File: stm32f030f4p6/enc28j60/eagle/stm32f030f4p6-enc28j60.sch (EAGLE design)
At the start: 29 parts, among them IC2 LM1117IDTX-3.3, IC3 LP2950, X1 MINI-USB-UX60-MB-5ST

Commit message: updated stm32f030f4p6/enc28j60/eagle
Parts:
- added BOOT-SW: (no value), pinhead:PINHD-1X3
- added R1: 5K, resistor:R-EU_0204/5
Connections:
- net N$1 renamed VDDA
- net N$10 renamed PA3
- net N$11 renamed PA4@L
- net N$12 renamed PA5
- net N$13 renamed PA6
- net N$14 renamed PF1@LED
- net N$187 renamed 5V@EXT
- net N$188 renamed 3V3@EXT
- net N$19 renamed PF1@OCC
- net N$190 renamed PA7
- net N$20 renamed PF0@OCC
- net N$21 renamed RESET
- net N$23 renamed PA4@R
- net N$29 renamed PF0@LED
- net N$4 renamed PF0
- net N$5 renamed PF1
- net N$6 renamed PA4
- net N$7 renamed PA0
- net N$8 renamed PA1
- net N$9 renamed PA2
- removed net N$3: STM32F030F4PX_L.1, STM32F030F4PX_L.2
- new net BOOT: R1.1, STM32F030F4PX_L.1, STM32F030F4PX_L.2
- new net N$1: BOOT-SW.2, R1.2
- net GND@0: now also BOOT-SW.1
- net VDD: now also BOOT-SW.3
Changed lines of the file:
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@@
 <part name="LED3" library="eagle-ltspice" deviceset="LED_E" device="LD260"/>
 <part name="LED1_R1" library="resistor" deviceset="R-EU_" device="0204/7"/>
+<part name="BOOT-SW" library="pinhead" deviceset="PINHD-1X3" device=""/>
+<part name="R1" library="resistor" deviceset="R-EU_" device="0204/5" value="5K"/>
 </parts>
 <sheets>
@@
 <instance part="LED3" gate="G$1" x="124.46" y="93.98"/>
 <instance part="LED1_R1" gate="G$1" x="119.38" y="88.9"/>
+<instance part="BOOT-SW" gate="A" x="119.38" y="33.02" rot="R90"/>
+<instance part="R1" gate="G$1" x="116.84" y="35.56"/>
 </instances>
 <busses>
 </busses>
 <nets>
-<net name="N$1" class="0">
+<net name="VDDA" class="0">
 <segment>
 <pinref part="STM32F030F4PX_L" gate="A" pin="9"/>
@@
 </segment>
 </net>
-<net name="N$3" class="0">
+<net name="BOOT" class="0">
 <segment>
 <pinref part="STM32F030F4PX_L" gate="A" pin="1"/>
 <pinref part="STM32F030F4PX_L" gate="A" pin="2"/>
-<wire x1="101.6" y1="53.34" x2="106.68" y2="53.34" width="0.1524" layer="91"/>
-<wire x1="99.06" y1="53.34" x2="101.6" y2="53.34" width="0.1524" layer="91"/>
+<wire x1="99.06" y1="53.34" x2="106.68" y2="53.34" width="0.1524" layer="91"/>
 <junction x="99.06" y="53.34"/>
 <junction x="106.68" y="53.34"/>
-</segment>
-</net>
-<net name="N$4" class="0">
+<wire x1="106.68" y1="53.34" x2="111.76" y2="53.34" width="0.1524" layer="91"/>
+<wire x1="111.76" y1="53.34" x2="111.76" y2="35.56" width="0.1524" layer="91"/>
+<pinref part="R1" gate="G$1" pin="1"/>
+</segment>
+</net>
+<net name="PF0" class="0">
 <segment>
 <pinref part="STM32F030F4PX_L" gate="A" pin="4"/>
@@
 </segment>
 </net>
-<net name="N$5" class="0">
+<net name="PF1" class="0">
 <segment>
 <pinref part="STM32F030F4PX_L" gate="A" pin="5"/>
@@
 </segment>
 </net>
-<net name="N$7" class="0">
+<net name="PA0" class="0">
 <segment>
 <pinref part="STM32F030F4PX_L" gate="A" pin="12"/>
@@
 </segment>
 </net>
-<net name="N$8" class="0">
+<net name="PA1" class="0">
 <segment>
 <pinref part="STM32F030F4PX_L" gate="A" pin="13"/>
@@
 </segment>
 </net>
-<net name="N$9" class="0">
+<net name="PA2" class="0">
 <segment>
 <pinref part="STM32F030F4PX_L" gate="A" pin="16"/>
@@
 </segment>
 </net>
-<net name="N$10" class="0">
+<net name="PA3" class="0">
 <segment>
 <pinref part="STM32F030F4PX_L" gate="A" pin="17"/>
@@
 </segment>
 </net>
-<net name="N$11" class="0">
+<net name="PA4@L" class="0">
 <segment>
 <wire x1="99.06" y1="-7.62" x2="5.08" y2="-7.62" width="0.1524" layer="91"/>
@@
 </segment>
 </net>
-<net name="N$12" class="0">
+<net name="PA5" class="0">
 <segment>
 <pinref part="STM32F030F4PX_R" gate="A" pin="19"/>
@@
 </segment>
 </net>
-<net name="N$13" class="0">
+<net name="PA6" class="0">
 <segment>
 <pinref part="STM32F030F4PX_R" gate="A" pin="18"/>
@@
 </segment>
 </net>
-<net name="N$21" class="0">
+<net name="RESET" class="0">
 <segment>
 <pinref part="RST_S" gate="S" pin="2"/>
@@
 <wire x1="101.6" y1="66.04" x2="86.36" y2="66.04" width="0.1524" layer="91"/>
 <junction x="86.36" y="66.04"/>
-<wire x1="86.36" y1="25.4" x2="132.08" y2="25.4" width="0.1524" layer="91"/>
+<wire x1="86.36" y1="25.4" x2="116.84" y2="25.4" width="0.1524" layer="91"/>
+<wire x1="116.84" y1="25.4" x2="132.08" y2="25.4" width="0.1524" layer="91"/>
 <wire x1="132.08" y1="25.4" x2="132.08" y2="40.64" width="0.1524" layer="91"/>
 <junction x="86.36" y="25.4"/>
@@
 <pinref part="LED1_R1" gate="G$1" pin="1"/>
 <wire x1="114.3" y1="88.9" x2="109.22" y2="88.9" width="0.1524" layer="91"/>
+<pinref part="BOOT-SW" gate="A" pin="1"/>
+<wire x1="116.84" y1="30.48" x2="116.84" y2="25.4" width="0.1524" layer="91"/>
+<junction x="116.84" y="25.4"/>
 </segment>
 </net>
@@
 <pinref part="VDD{,A}" gate="G$1" pin="1"/>
 <pinref part="STM32F030F4PX_R" gate="A" pin="9"/>
-<wire x1="124.46" y1="43.18" x2="137.16" y2="43.18" width="0.1524" layer="91"/>
+<wire x1="124.46" y1="43.18" x2="129.54" y2="43.18" width="0.1524" layer="91"/>
 <pinref part="STM32F030F4PX_R" gate="A" pin="10"/>
+<wire x1="129.54" y1="43.18" x2="137.16" y2="43.18" width="0.1524" layer="91"/>
 <wire x1="137.16" y1="43.18" x2="144.78" y2="43.18" width="0.1524" layer="91"/>
 <junction x="137.16" y="43.18"/>
@@
 <pinref part="LED3" gate="G$1" pin="A"/>
 <junction x="124.46" y="96.52"/>
-</segment>
-</net>
-<net name="N$6" class="0">
+<pinref part="BOOT-SW" gate="A" pin="3"/>
+<wire x1="121.92" y1="30.48" x2="129.54" y2="30.48" width="0.1524" layer="91"/>
+<wire x1="129.54" y1="30.48" x2="129.54" y2="43.18" width="0.1524" layer="91"/>
+<junction x="129.54" y="43.18"/>
+</segment>
+</net>
+<net name="PA4" class="0">
 <segment>
 <pinref part="STM32F030F4PX_L" gate="A" pin="19"/>
@@
 </segment>
 </net>
-<net name="N$23" class="0">
+<net name="PA4@R" class="0">
 <segment>
 <pinref part="PA4_JP" gate="A" pin="3"/>
@@
 </segment>
 </net>
-<net name="N$29" class="0">
+<net name="PF0@LED" class="0">
 <segment>
 <pinref part="LED2_R" gate="G$1" pin="2"/>
@@
 </segment>
 </net>
-<net name="N$187" class="0">
+<net name="5V@EXT" class="0">
 <segment>
 <pinref part="ENC_PW" gate="A" pin="3"/>
@@
 </segment>
 </net>
-<net name="N$188" class="0">
+<net name="3V3@EXT" class="0">
 <segment>
 <pinref part="ENC_PW" gate="A" pin="1"/>
@@
 </segment>
 </net>
-<net name="N$190" class="0">
+<net name="PA7" class="0">
 <segment>
 <pinref part="ENC28J60" gate="A" pin="5"/>
@@
 </segment>
 </net>
-<net name="N$14" class="0">
+<net name="PF1@LED" class="0">
 <segment>
 <pinref part="LED1_R" gate="G$1" pin="2"/>
@@
 </segment>
 </net>
-<net name="N$19" class="0">
+<net name="PF1@OCC" class="0">
 <segment>
 <pinref part="LED1_JP" gate="A" pin="1"/>
@@
 </segment>
 </net>
-<net name="N$20" class="0">
+<net name="PF0@OCC" class="0">
 <segment>
 <pinref part="LED2_JP" gate="A" pin="3"/>
@@
 </segment>
 </net>
+<net name="N$1" class="0">
+<segment>
+<pinref part="R1" gate="G$1" pin="2"/>
+<wire x1="121.92" y1="35.56" x2="119.38" y2="33.02" width="0.1524" layer="91"/>
+<pinref part="BOOT-SW" gate="A" pin="2"/>
+<wire x1="119.38" y1="33.02" x2="119.38" y2="30.48" width="0.1524" layer="91"/>
+</segment>
+</net>

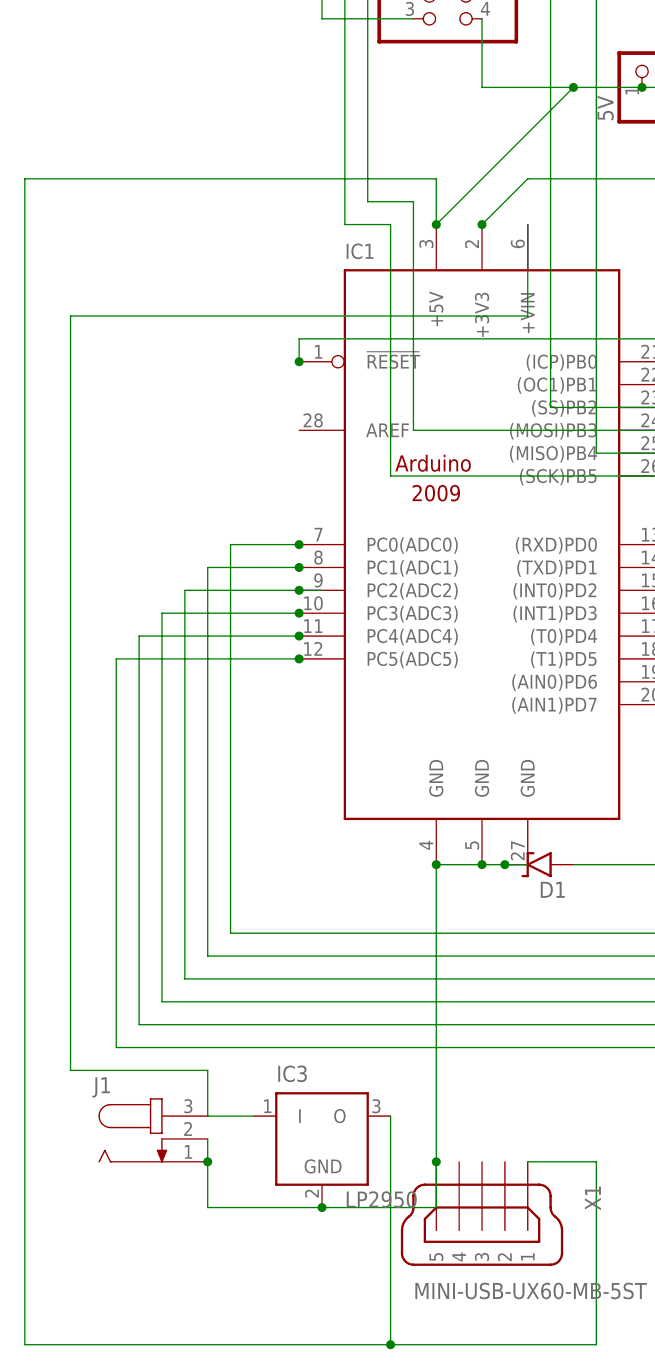
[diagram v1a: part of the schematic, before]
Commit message: Updated stm32f030f4p6/enc28j60/eagle
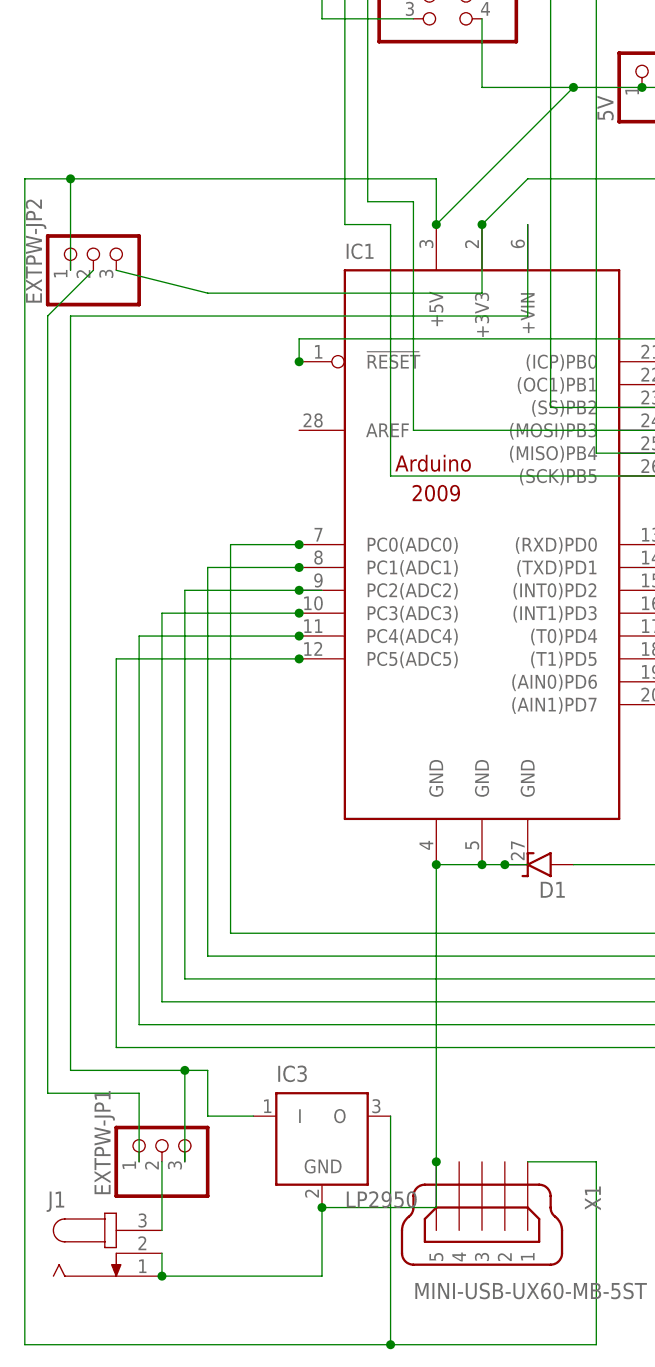
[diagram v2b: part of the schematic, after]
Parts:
- added EXTPW-JP1, EXTPW-JP2: (no value), pinhead:PINHD-1X3
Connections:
- net N$1 renamed BOOT@R
- removed net N$24: IC1.+VIN, IC3.I, J1.3
- new net VIN: EXTPW-JP1.2, J1.3
- new net VIN@HIGH: EXTPW-JP1.3, IC1.+VIN, IC3.I
- new net VIN@LOW: EXTPW-JP1.1, EXTPW-JP2.2
- net 5V: now also EXTPW-JP2.1
- net VDD: now also EXTPW-JP2.3
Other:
- moved on the sheet: J1
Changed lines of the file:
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@@
 <part name="BOOT-SW" library="pinhead" deviceset="PINHD-1X3" device=""/>
 <part name="R1" library="resistor" deviceset="R-EU_" device="0204/5" value="5K"/>
+<part name="EXTPW-JP1" library="pinhead" deviceset="PINHD-1X3" device=""/>
+<part name="EXTPW-JP2" library="pinhead" deviceset="PINHD-1X3" device=""/>
 </parts>
 <sheets>
@@
 <instance part="D1" gate="G$1" x="50.8" y="10.16" rot="R180"/>
 <instance part="X1" gate="G$1" x="43.18" y="-27.94" rot="R270"/>
-<instance part="J1" gate="G$1" x="7.62" y="-20.32"/>
+<instance part="J1" gate="G$1" x="2.54" y="-33.02"/>
 <instance part="IC3" gate="G$1" x="25.4" y="-20.32"/>
 <instance part="Q1" gate="G$1" x="132.08" y="66.04" rot="R270"/>
@@
 <instance part="BOOT-SW" gate="A" x="119.38" y="33.02" rot="R90"/>
 <instance part="R1" gate="G$1" x="116.84" y="35.56"/>
+<instance part="EXTPW-JP1" gate="A" x="7.62" y="-20.32" rot="R90"/>
+<instance part="EXTPW-JP2" gate="A" x="0" y="78.74" rot="R90"/>
 </instances>
 <busses>
@@
 <wire x1="33.02" y1="-43.18" x2="-7.62" y2="-43.18" width="0.1524" layer="91"/>
 <wire x1="-7.62" y1="-43.18" x2="-7.62" y2="86.36" width="0.1524" layer="91"/>
-<wire x1="-7.62" y1="86.36" x2="38.1" y2="86.36" width="0.1524" layer="91"/>
+<wire x1="-7.62" y1="86.36" x2="-2.54" y2="86.36" width="0.1524" layer="91"/>
+<wire x1="-2.54" y1="86.36" x2="38.1" y2="86.36" width="0.1524" layer="91"/>
 <wire x1="38.1" y1="86.36" x2="38.1" y2="81.28" width="0.1524" layer="91"/>
 <pinref part="IC3" gate="G$1" pin="O"/>
 <wire x1="33.02" y1="-17.78" x2="33.02" y2="-43.18" width="0.1524" layer="91"/>
 <junction x="33.02" y="-43.18"/>
+<pinref part="EXTPW-JP2" gate="A" pin="1"/>
+<wire x1="-2.54" y1="76.2" x2="-2.54" y2="86.36" width="0.1524" layer="91"/>
+<junction x="-2.54" y="86.36"/>
 </segment>
 </net>
@@
 <wire x1="129.54" y1="30.48" x2="129.54" y2="43.18" width="0.1524" layer="91"/>
 <junction x="129.54" y="43.18"/>
+<pinref part="EXTPW-JP2" gate="A" pin="3"/>
+<wire x1="2.54" y1="76.2" x2="12.7" y2="73.66" width="0.1524" layer="91"/>
+<wire x1="12.7" y1="73.66" x2="43.18" y2="73.66" width="0.1524" layer="91"/>
+<wire x1="43.18" y1="73.66" x2="43.18" y2="81.28" width="0.1524" layer="91"/>
 </segment>
 </net>
@@
 <pinref part="J1" gate="G$1" pin="2"/>
 <pinref part="J1" gate="G$1" pin="1"/>
-<wire x1="12.7" y1="-20.32" x2="12.7" y2="-22.86" width="0.1524" layer="91"/>
+<wire x1="7.62" y1="-33.02" x2="7.62" y2="-35.56" width="0.1524" layer="91"/>
 <pinref part="IC3" gate="G$1" pin="GND"/>
-<wire x1="25.4" y1="-27.94" x2="12.7" y2="-27.94" width="0.1524" layer="91"/>
-<wire x1="12.7" y1="-27.94" x2="12.7" y2="-22.86" width="0.1524" layer="91"/>
-<junction x="12.7" y="-22.86"/>
+<wire x1="25.4" y1="-27.94" x2="25.4" y2="-35.56" width="0.1524" layer="91"/>
+<wire x1="25.4" y1="-35.56" x2="7.62" y2="-35.56" width="0.1524" layer="91"/>
+<junction x="7.62" y="-35.56"/>
 <pinref part="IC1" gate="G$1" pin="GND@3"/>
 <pinref part="IC1" gate="G$1" pin="GND@2"/>
@@
 </segment>
 </net>
-<net name="N$24" class="0">
+<net name="VIN@HIGH" class="0">
 <segment>
 <pinref part="IC3" gate="G$1" pin="I"/>
-<pinref part="J1" gate="G$1" pin="3"/>
 <wire x1="17.78" y1="-17.78" x2="12.7" y2="-17.78" width="0.1524" layer="91"/>
 <wire x1="12.7" y1="-17.78" x2="12.7" y2="-12.7" width="0.1524" layer="91"/>
-<wire x1="12.7" y1="-12.7" x2="-2.54" y2="-12.7" width="0.1524" layer="91"/>
+<wire x1="12.7" y1="-12.7" x2="10.16" y2="-12.7" width="0.1524" layer="91"/>
+<wire x1="10.16" y1="-12.7" x2="-2.54" y2="-12.7" width="0.1524" layer="91"/>
 <wire x1="-2.54" y1="-12.7" x2="-2.54" y2="71.12" width="0.1524" layer="91"/>
 <pinref part="IC1" gate="G$1" pin="+VIN"/>
 <wire x1="-2.54" y1="71.12" x2="48.26" y2="71.12" width="0.1524" layer="91"/>
 <wire x1="48.26" y1="71.12" x2="48.26" y2="81.28" width="0.1524" layer="91"/>
+<pinref part="EXTPW-JP1" gate="A" pin="3"/>
+<wire x1="10.16" y1="-22.86" x2="10.16" y2="-12.7" width="0.1524" layer="91"/>
+<junction x="10.16" y="-12.7"/>
 </segment>
 </net>
@@
 </segment>
 </net>
-<net name="N$1" class="0">
+<net name="BOOT@R" class="0">
 <segment>
 <pinref part="R1" gate="G$1" pin="2"/>
@@
 </segment>
 </net>
+<net name="VIN" class="0">
+<segment>
+<pinref part="J1" gate="G$1" pin="3"/>
+<pinref part="EXTPW-JP1" gate="A" pin="2"/>
+<wire x1="7.62" y1="-30.48" x2="7.62" y2="-22.86" width="0.1524" layer="91"/>
+</segment>
+</net>
+<net name="VIN@LOW" class="0">
+<segment>
+<pinref part="EXTPW-JP2" gate="A" pin="2"/>
+<wire x1="0" y1="76.2" x2="-5.08" y2="71.12" width="0.1524" layer="91"/>
+<wire x1="-5.08" y1="71.12" x2="-5.08" y2="-15.24" width="0.1524" layer="91"/>
+<wire x1="-5.08" y1="-15.24" x2="5.08" y2="-15.24" width="0.1524" layer="91"/>
+<pinref part="EXTPW-JP1" gate="A" pin="1"/>
+<wire x1="5.08" y1="-15.24" x2="5.08" y2="-22.86" width="0.1524" layer="91"/>
+</segment>
+</net>

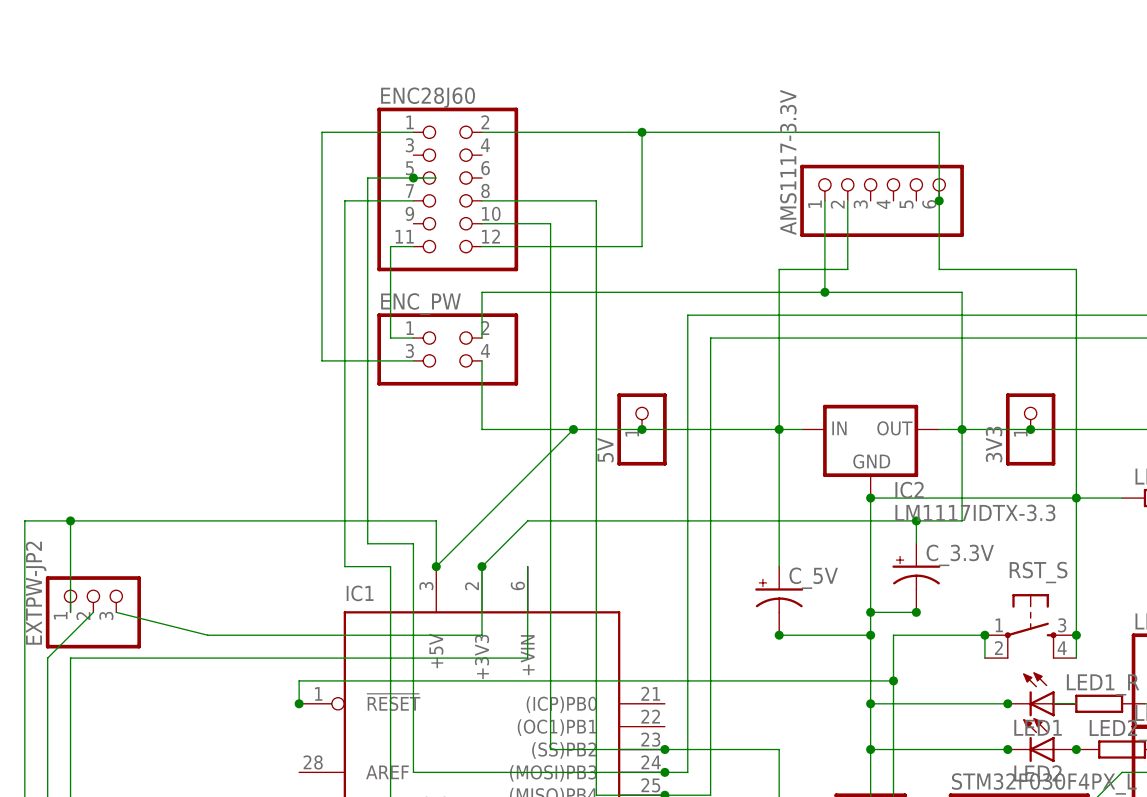
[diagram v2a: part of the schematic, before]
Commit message: Connected enc28j60 RST in stm32f030f4p6/enc28j60/eagle
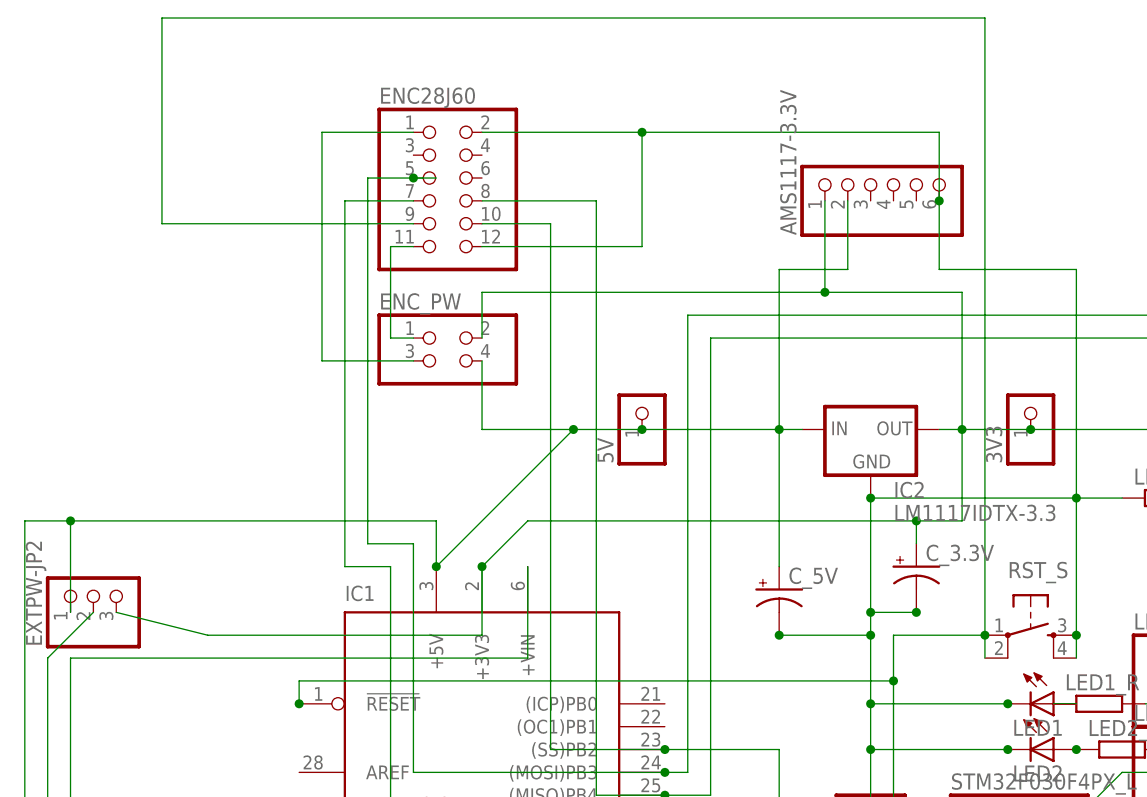
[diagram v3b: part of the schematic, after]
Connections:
- net RESET: now also ENC28J60.9
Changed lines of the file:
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@@
 <junction x="88.9" y="68.58"/>
 <junction x="22.86" y="66.04"/>
+<pinref part="ENC28J60" gate="A" pin="9"/>
+<wire x1="35.56" y1="119.38" x2="7.62" y2="119.38" width="0.1524" layer="91"/>
+<wire x1="7.62" y1="119.38" x2="7.62" y2="142.24" width="0.1524" layer="91"/>
+<wire x1="7.62" y1="142.24" x2="99.06" y2="142.24" width="0.1524" layer="91"/>
+<wire x1="99.06" y1="142.24" x2="99.06" y2="73.66" width="0.1524" layer="91"/>
 </segment>
 </net>
